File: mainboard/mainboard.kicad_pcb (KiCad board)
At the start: 2 copper layers, 68 x 87.8 mm, 74 parts, among them J1 Servo, J2 ADC Pins, J3 USB Data, J4 Button Interface, J5 Power, J6 Release Button, J7 GPIO Pins, Q1 BSS138, Q2 2N7002, Q3 2N7002, Q4 2N7002, Q5 2N7002, Q6 2N7002, SW1 SW_Push, U1 RP2040, U2 W25Q128JVS, U3 RV-3028-C7, U4 ITR9608-F, U5 TCA9535RTWR, U6 LTC-4627JD, Y1 Crystal_ABM8

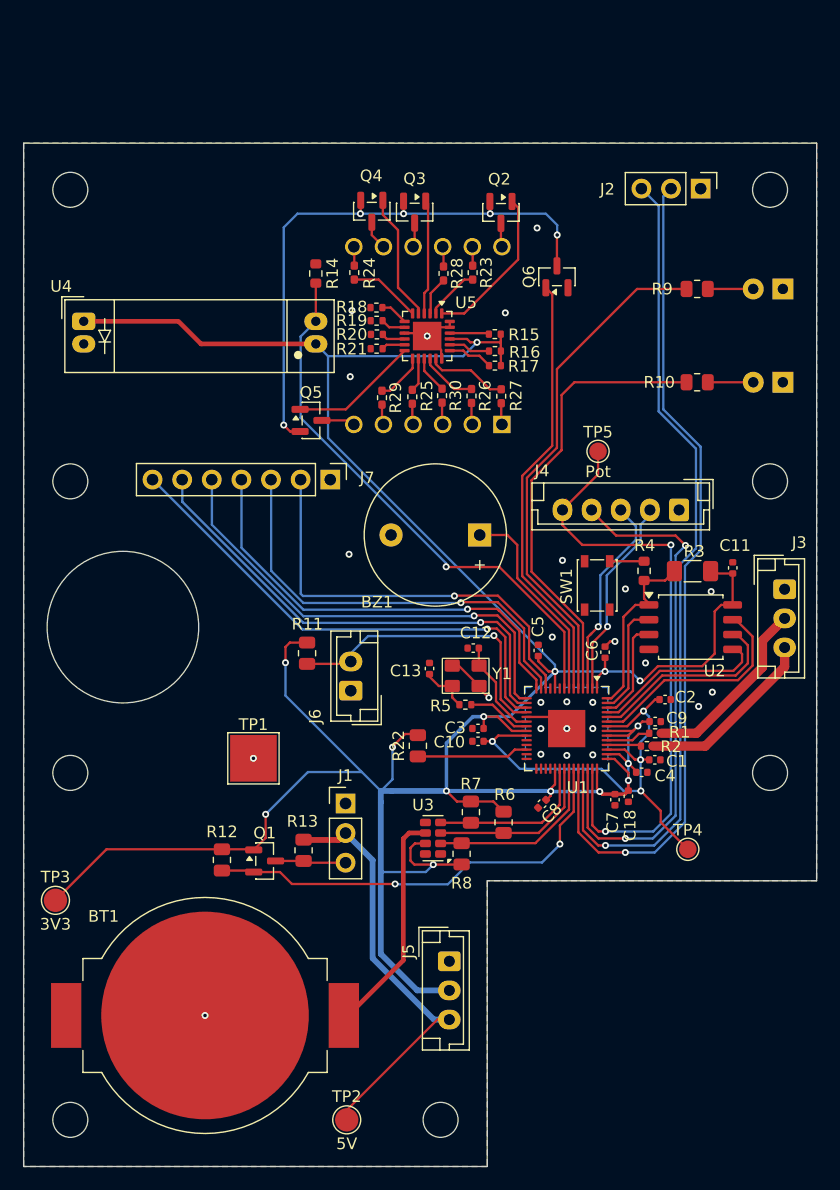
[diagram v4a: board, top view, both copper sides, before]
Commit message: replaced ports with clik-mate, moved flash storage to accommodate. Organized traces Replaced FETs
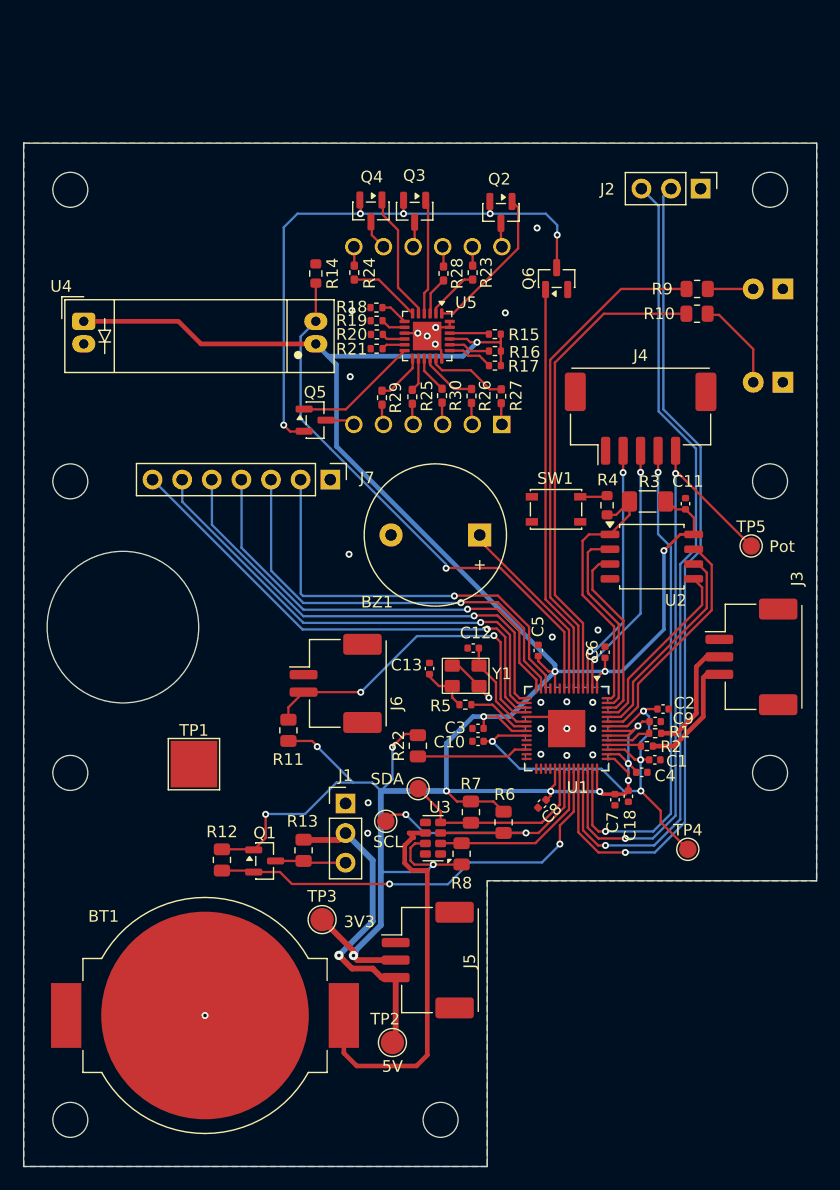
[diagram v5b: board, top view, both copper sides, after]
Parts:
- added SCL: Pot, TestPoint:TestPoint_Pad_D1.5mm, F.Cu at (108.8, 114.4)
- added SDA: Pot, TestPoint:TestPoint_Pad_D1.5mm, F.Cu at (111.6, 111.6)
- J3, J5: footprint Connector_JST:JST_EH_B3B-EH-A_1x03_P2.50mm_Vertical -> Connector_Molex:Molex_CLIK-Mate_505405-0370_1x03-1MP_P1.50mm_Vertical
- J4: footprint Connector_JST:JST_EH_B5B-EH-A_1x05_P2.50mm_Vertical -> Connector_Molex:Molex_CLIK-Mate_505405-0570_1x05-1MP_P1.50mm_Vertical
- J6: footprint Connector_JST:JST_EH_B2B-EH-A_1x02_P2.50mm_Vertical -> Connector_Molex:Molex_CLIK-Mate_505405-0270_1x02-1MP_P1.50mm_Vertical
- Q2, Q3, Q4, Q5, Q6: value 2N7002 -> BSS138
- moved TP3 22.9 mm to (103.3, 122.8)
- moved TP5 15.4 mm to (140.1, 90.8)
- moved J4 8.49 mm to (130.7, 79.9), turned to 0 degrees
- moved TP2 7.70 mm to (109.4, 133.4)
- moved SW1 7.42 mm to (123.4, 87.7), turned to 0 degrees
- moved R3 7.11 mm to (131.2, 87.0)
- moved U2 6.91 mm to (131.6, 91.7)
- moved C11 6.83 mm to (134.5, 87.2)
- moved R11 6.80 mm to (100.5, 106.6), turned to 90 degrees
- moved J3 6.46 mm to (140.2, 100.3)
- moved R4 6.46 mm to (127.8, 87.3)
- moved R10 5.88 mm to (135.5, 70.9)
- moved TP1 5.12 mm to (92.3, 109.5)
- moved J5 1.85 mm to (112.4, 126.3)
- moved J6 1.44 mm to (104.5, 102.6), turned to -90 degrees
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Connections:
- U1 pad 2: /AIN1 -> /AIN2
- U1 pad 3: /AIN2 -> /AIN1
- U1 pad 40: /BTNS -> /POT
- U1 pad 41: /POT -> /BTNS
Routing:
- net +3.3V: track 272.7 -> 249.1 mm, vias 15 -> 16
- net Net-(BT1-+): track 19.6 -> 33.8 mm
- net /RTC_SCL: track 14.8 -> 27.7 mm, vias 0 -> 2
- net +5V: track 37.2 -> 27.8 mm, vias 0 -> 1
- net /QSPI_SS: track 15.6 -> 23.6 mm
- net /QSPI_SD1: track 9.73 -> 16.8 mm
- net /QSPI_SD2: track 8.84 -> 15.6 mm
- net /USB D+: track 16.1 -> 10.0 mm
- net /USB D-: track 15.8 -> 10.2 mm
- net /AIN1: track 17.3 -> 21.9 mm, vias 1 -> 2
- net /AIN2: track 17.7 -> 22.2 mm, vias 1 -> 2
- net /B_RELEASE: track 25.5 -> 29.6 mm, vias 1 -> 2
- net Net-(D2-A): track 3.90 -> 7.97 mm
- net /RTC_SDA: track 14.0 -> 17.7 mm
- net /RED_LED: track 39.5 -> 42.1 mm
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
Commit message: Reorganized many components per CAD implementation feedback. Repositioned photointerrupt, and RP2040 and local parts, Reduced extra GPIO pins & repositioned other connectors
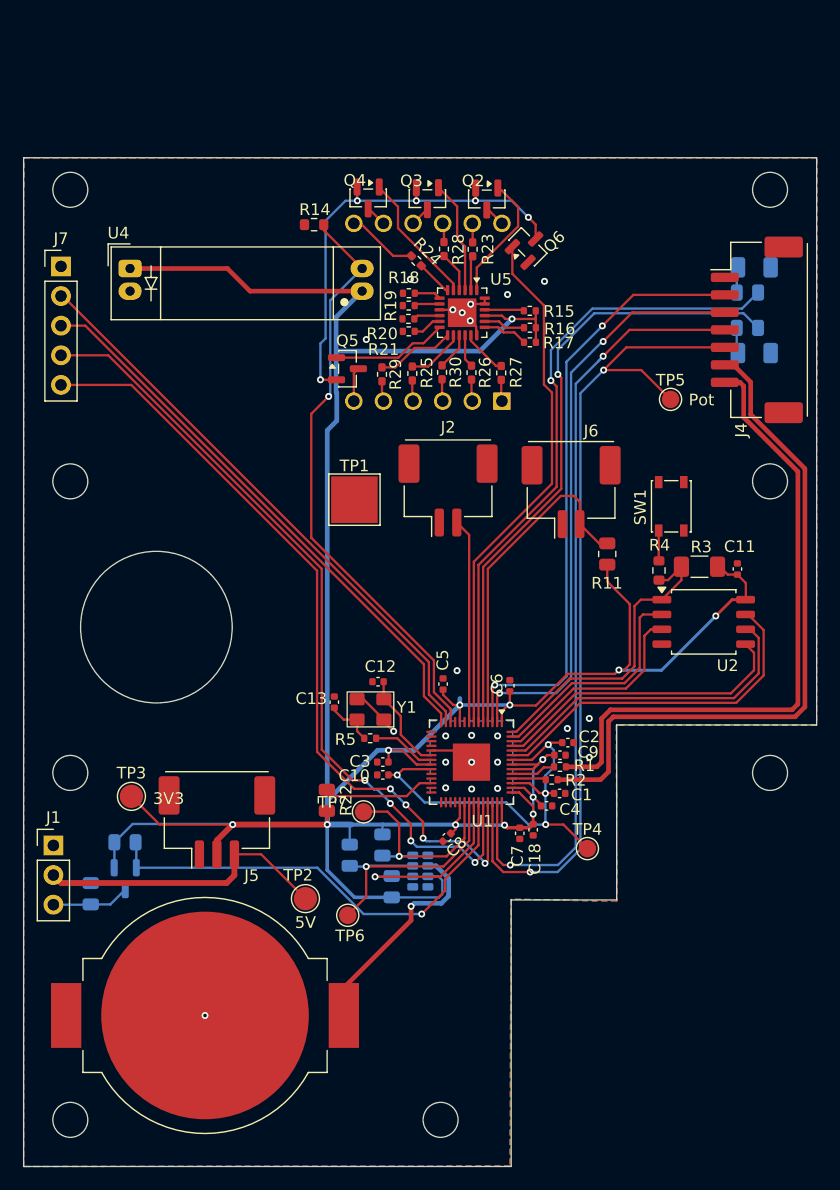
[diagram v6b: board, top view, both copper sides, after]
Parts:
- removed BZ1: Buzzer, Buzzer_Beeper:Buzzer_12x9.5RM7.6
- removed J3: USB Data, Connector_Molex:Molex_CLIK-Mate_505405-0370_1x03-1MP_P1.50mm_Vertical
- D1, D2: footprint LED_THT:LED_D3.0mm -> LED_SMD:LED_1206_3216Metric
- J2: value ADC Pins -> Buzzer; footprint Connector_PinHeader_2.54mm:PinHeader_1x03_P2.54mm_Vertical -> Connector_Molex:Molex_CLIK-Mate_505405-0270_1x02-1MP_P1.50mm_Vertical
- J4: footprint Connector_Molex:Molex_CLIK-Mate_505405-0570_1x05-1MP_P1.50mm_Vertical -> Connector_Molex:Molex_CLIK-Mate_505405-0770_1x07-1MP_P1.50mm_Vertical
- J7: value GPIO Pins -> Extra Pins; footprint Connector_PinHeader_2.54mm:PinHeader_1x07_P2.54mm_Vertical -> Connector_PinHeader_2.54mm:PinHeader_1x05_P2.54mm_Vertical
- Q1, R10, R12, R13, R6, R7, R8, R9, U3: moved to B.Cu
- moved J2 33.7 mm to (114.1, 86.0), turned to 0 degrees
- moved R11 31.2 mm to (127.8, 91.5)
- moved J7 29.5 mm to (81.0, 66.8), turned to 0 degrees
- moved TP1 26.5 mm to (106.1, 86.8)
- moved J6 26.0 mm to (124.7, 86.2), turned to 0 degrees
- moved J1 25.3 mm to (80.3, 116.5)
- moved J5 21.6 mm to (94.3, 114.5), turned to 0 degrees
- moved TP3 19.5 mm to (87.0, 112.3)
- moved R13 18.6 mm to (83.5, 120.6)
- moved TP2 14.4 mm to (101.9, 121.0)
- moved TP5 14.3 mm to (133.2, 78.2)
- moved R6 13.5 mm to (105.7, 117.3)
- moved J4 12.5 mm to (140.6, 72.3), turned to -90 degrees
- moved Q1 12.0 mm to (86.5, 119.3), turned to -90 degrees
- moved SW1 9.88 mm to (133.3, 87.4), turned to 90 degrees
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- renumbered SCL to TP6, SDA to TP7
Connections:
- J2 pad 2: /GPIO26_ADC0 -> /Buzzer
- J7 pad 4: /GPIO11 -> /GPIO26_ADC0
- J7 pad 5: /GPIO12 -> /GPIO27_ADC1
- U1 pad 12: /GPIO9 -> /IR
- U1 pad 13: /GPIO10 -> /GPIO9
- U1 pad 14: /GPIO11 -> /GPIO10
- U1 pad 15: /GPIO12 -> unconnected-(U1-GPIO12-Pad15)
- U1 pad 16: /GPIO13 -> unconnected-(U1-GPIO13-Pad16)
- U1 pad 17: /GPIO14 -> unconnected-(U1-GPIO14-Pad17)
- U1 pad 18: /B_RELEASE -> unconnected-(U1-GPIO15-Pad18)
- U1 pad 4: /RED_LED -> /B_RELEASE
- U1 pad 5: /WHITE_LED -> /RED_LED
- U1 pad 6: /7-SEG_PWM -> /WHITE_LED
- U1 pad 7: /Buzzer -> /7-SEG_PWM
- U1 pad 8: /IR -> /Buzzer
- U5 pad 3: /7-Segment/LED_f -> /7-Segment/CC2
- U5 pad 4: /7-Segment/CC2 -> /7-Segment/LED_f
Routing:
- net /USB D-: track 10.2 -> 58.9 mm
- net /USB D+: track 10.0 -> 55.2 mm
- net /GPIO14: track 43.2 -> 0.00 mm, vias 1 -> 0
- net /GPIO13: track 41.7 -> 0.00 mm, vias 1 -> 0
- net /GPIO12: track 40.2 -> 0.00 mm, vias 1 -> 0
- net /GPIO11: track 38.2 -> 0.00 mm, vias 1 -> 0
- net /AIN1: track 21.9 -> 52.6 mm
- net /AIN2: track 22.2 -> 50.8 mm
- net /BTNS: track 44.2 -> 67.5 mm
- net /POT: track 54.1 -> 73.7 mm
- net Net-(BT1-+): track 33.8 -> 19.1 mm, vias 0 -> 1
- net /GPIO9: track 36.4 -> 50.3 mm, vias 1 -> 0
- net +3.3V: track 249.1 -> 261.4 mm, vias 16 -> 13
- net /RED_LED: track 42.1 -> 53.9 mm, vias 0 -> 1
- net /WHITE_LED: track 43.4 -> 54.8 mm, vias 0 -> 1
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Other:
- board size 68 x 87.8 mm -> 68 x 86.5 mm
